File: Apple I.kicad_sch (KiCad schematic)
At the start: 16 parts, among them J4 Processor Bus Connector, SW1 Reset, U1 W65C02SxP, U2 74125, U3 UT62256CPCL, U4 W27C512, U5 SN74HC00N, U6 74154, U7 74HC138, Y1 TXC-7C

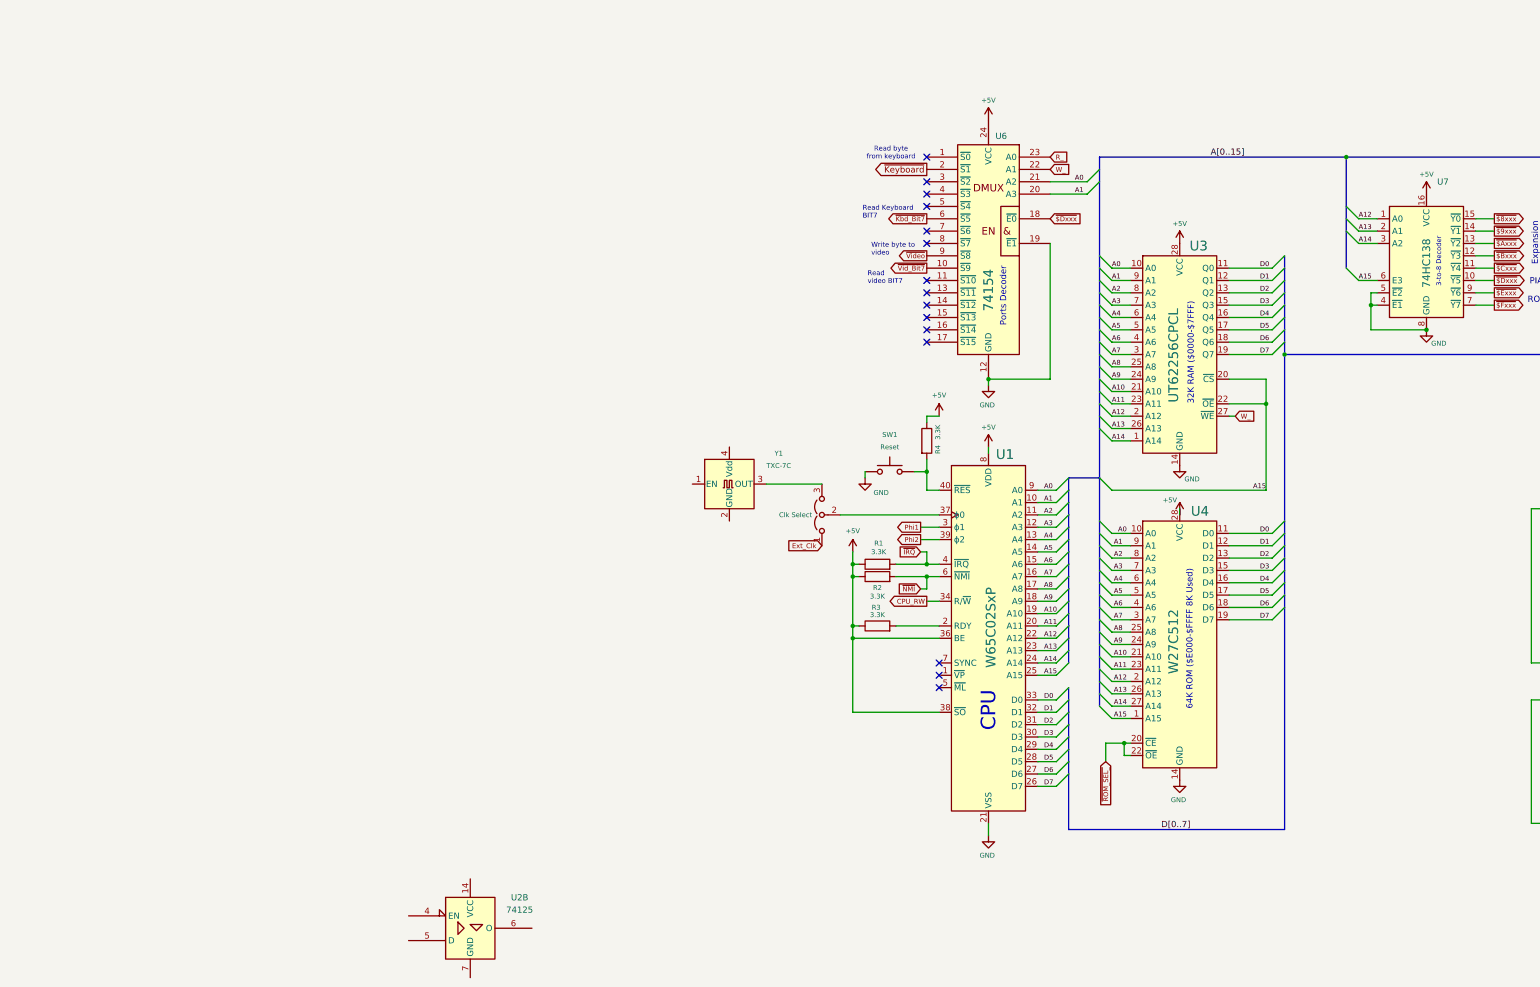
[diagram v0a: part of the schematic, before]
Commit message: Working on Video and Keyboard controllers
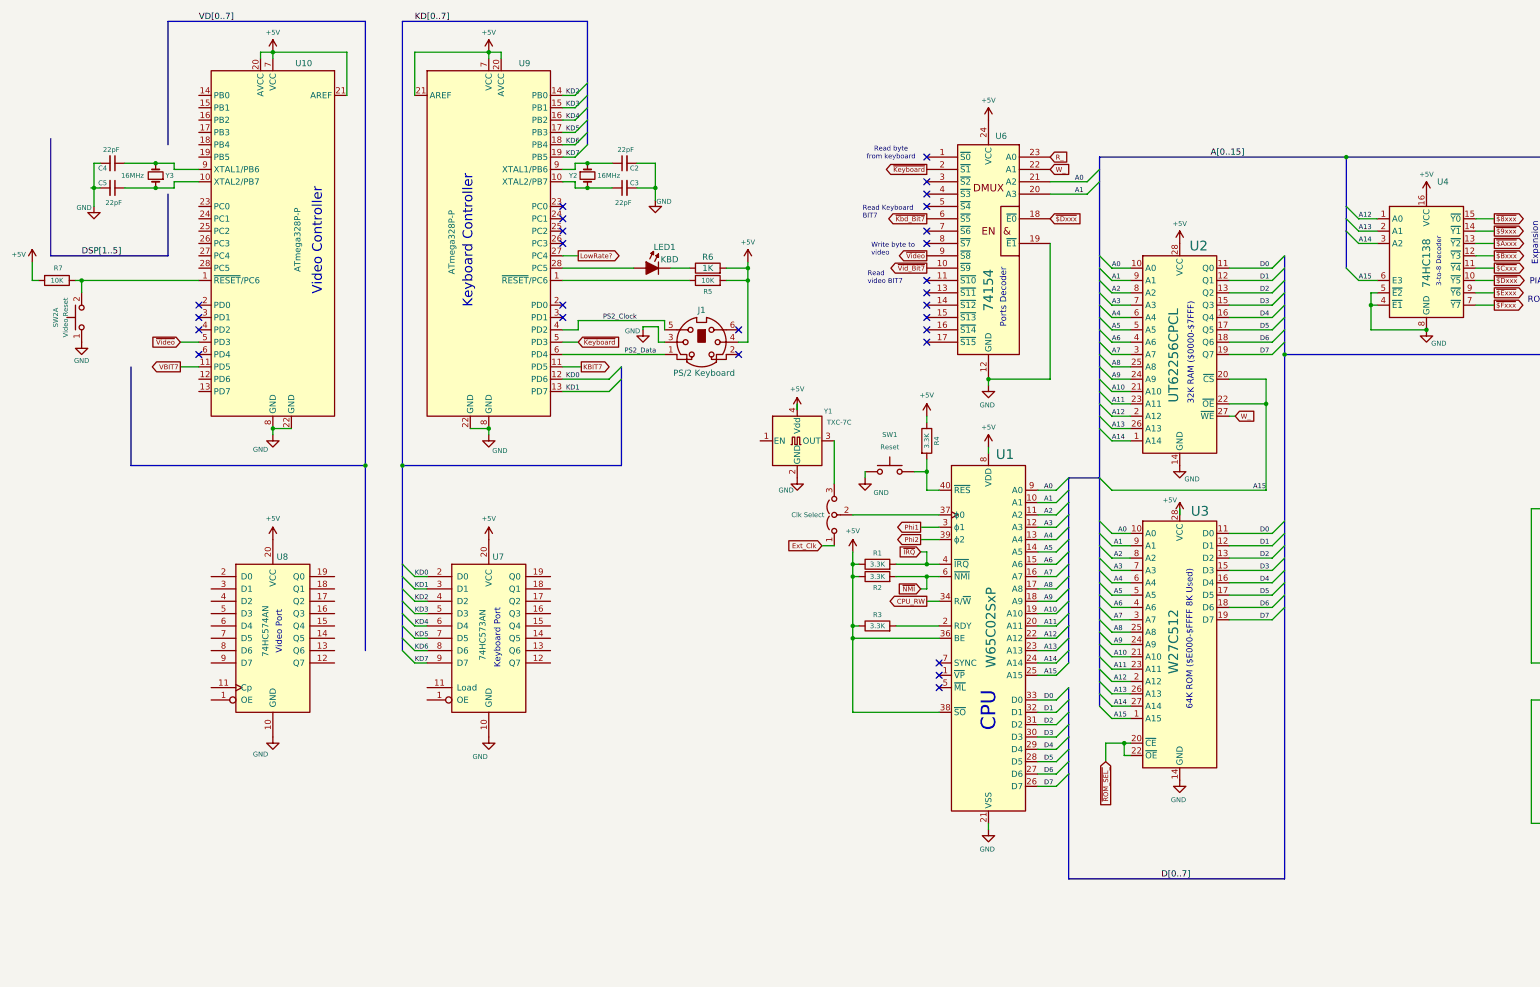
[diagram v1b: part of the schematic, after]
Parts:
- removed U2: 74125, symbol 74xx_IEEE:74125
- added C2, C3, C4, C5: 22pF, symbol Device:C_Small
- added J1: PS/2 Keyboard, symbol Connector:Mini-DIN-6
- added LED1: KBD, PCM_LED_THT_AKL:LED_D2.0mm_W4.8mm_H2.5mm_FlatTop, symbol PCM_LED_AKL:LED_2mm
- added R5, R7: 10K, symbol Device:R
- added R6: 1K, symbol Device:R
- added SW2: Video Reset, symbol Switch:SW_Push_Dual_x2
- added U10, U9: ATmega328P-P, Package_DIP:DIP-28_W7.62mm, symbol MCU_Microchip_ATmega:ATmega328P-P
- added U7: 74HC573AN, symbol 74xx:74LS573
- added U8: 74HC574AN, symbol 74xx:74LS574
- added Y2, Y3: 16MHz, symbol Device:Crystal_Small
- renumbered U3 to U2, U4 to U3, U7 to U4
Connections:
- net +5V: now also Y1.4 (Vdd), J1.4, R5.2, R6.2, R7.2, U10.20 (AVCC), U10.21 (AREF), U10.7 (VCC), U7.20 (VCC), U8.20 (VCC), U9.20 (AVCC), U9.21 (AREF), U9.7 (VCC)
- net GND: now also Y1.2 (GND), C2.2, C3.2, C4.2, C5.2, J1.3, SW2.1 (C), U10.22 (GND), U10.8 (GND), U7.10 (GND), U8.10 (GND), U9.22 (GND), U9.8 (GND)
- net ~{Keyboard}: now also U9.5 (PD3)
- net ~{Video}: now also U10.5 (PD3)
- new net: C3.1, U9.10 (XTAL2/PB7), Y2.2
- new net: R7.1, SW2.2 (D), U10.1 (~{RESET}/PC6)
- new net: C5.1, U10.10 (XTAL2/PB7), Y3.1
- new net: C4.1, U10.9 (XTAL1/PB6), Y3.2
- new net: C2.1, U9.9 (XTAL1/PB6), Y2.1
- new net: R5.1, U9.1 (~{RESET}/PC6)
- new net: LED1.1 (K), R6.1
- new net: LED1.2 (A), U9.28 (PC5)
- new net KBIT7: U9.11 (PD5)
- new net KD0: U7.2 (D0), U9.12 (PD6)
- new net KD1: U7.3 (D1), U9.13 (PD7)
- new net KD2: U7.4 (D2), U9.14 (PB0)
- new net KD3: U7.5 (D3), U9.15 (PB1)
- new net KD4: U7.6 (D4), U9.16 (PB2)
- new net KD5: U7.7 (D5), U9.17 (PB3)
- new net KD6: U7.8 (D6), U9.18 (PB4)
- new net KD7: U7.9 (D7), U9.19 (PB5)
- new net LowRate?: U9.27 (PC4)
- new net PS2_Clock: J1.5, U9.4 (PD2)
- new net PS2_Data: J1.1, U9.6 (PD4)
- new net VBIT7: U10.11 (PD5)
- no-connect marks 15 -> 27
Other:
- note added: "Keyboard Controller"
- note added: "Keyboard Port"
- note added: "Video Controller"
- note added: "Video Port"
- moved on the sheet: Y1

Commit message: Schematic 1.0 add footprints and pcb
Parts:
- removed Y1: TXC-7C, Oscillator:Oscillator_SMD_TXC_7C-4Pin_5.0x3.2mm, symbol Oscillator:TXC-7C
- added C10, C11, C12, C13, C14, C15, C6, C7, C8, C9: .1uF, Capacitor_THT:C_Disc_D5.0mm_W2.5mm_P5.00mm, symbol Device:C_Small
- added JP2, JP3: AREF, Jumper:SolderJumper-2_P1.3mm_Open_RoundedPad1.0x1.5mm, symbol Jumper:SolderJumper_2_Open
- added R10, R11, R12, R8, R9: 10K, Resistor_THT:R_Axial_DIN0207_L6.3mm_D2.5mm_P10.16mm_Horizontal, symbol Device:R
- added unit 2 of SW2
- added TP1: Beep, TestPoint:TestPoint_THTPad_2.0x2.0mm_Drill1.0mm, symbol Connector:TestPoint
- added TP2: MISO, TestPoint:TestPoint_THTPad_2.0x2.0mm_Drill1.0mm, symbol Connector:TestPoint
- added TP3: TV-SDA, TestPoint:TestPoint_THTPad_2.0x2.0mm_Drill1.0mm, symbol Connector:TestPoint
- added TP4: TV-SCL, TestPoint:TestPoint_THTPad_2.0x2.0mm_Drill1.0mm, symbol Connector:TestPoint
- added TP5: LowRateClk, TestPoint:TestPoint_THTPad_2.0x2.0mm_Drill1.0mm, symbol Connector:TestPoint
- added U11: 2.8 TFT SPI 240x320 V1.2, digikey-footprints:TFT-320x240, symbol Driver_Display:CR2013-MI2120
- added U12: SN74AHC125N, Package_DIP:DIP-14_W7.62mm_Socket, symbol dk_Logic-Buffers-Drivers-Receivers-Transceivers:SN74AHCT125N
- added Y1: 1MHz, Oscillator:Oscillator_DIP-8, symbol Oscillator:CXO_DIP8
- C1: value 0.1uF -> .1uF; footprint (none) -> Capacitor_THT:C_Disc_D5.0mm_W2.5mm_P5.00mm
- C2, C3, C4, C5: footprint (none) -> Capacitor_THT:C_Disc_D5.0mm_W2.5mm_P5.00mm
- J1: footprint (none) -> digikey-footprints:MINI-DIN-6-FULL-SHIELD
- J4: footprint (none) -> Connector_PinHeader_2.54mm:PinHeader_2x24_P2.54mm_Vertical
- JP1: footprint (none) -> Connector_PinHeader_2.54mm:PinHeader_1x03_P2.54mm_Vertical
- R1, R2, R3, R4, R5, R6, R7: footprint (none) -> Resistor_THT:R_Axial_DIN0207_L6.3mm_D2.5mm_P10.16mm_Horizontal
- SW1, SW2: footprint (none) -> digikey-footprints:Terminal_Block_D1.3mm_P5mm
- U1: footprint Package_DIP:DIP-40_W15.24mm -> Package_DIP:DIP-40_W15.24mm_Socket
- U10, U9: footprint Package_DIP:DIP-28_W7.62mm -> Package_DIP:DIP-28_W7.62mm_Socket
- U2, U3: footprint Package_DIP:DIP-28_W15.24mm -> Package_DIP:DIP-28_W15.24mm_Socket
- U4: footprint (none) -> Package_DIP:DIP-16_W7.62mm_Socket
- U5: footprint digikey-footprints:DIP-14_W3mm -> Package_DIP:DIP-14_W7.62mm_Socket
- U6: footprint (none) -> Package_DIP:DIP-24_W7.62mm_Socket
- U7, U8: footprint (none) -> Package_DIP:DIP-20_W7.62mm_Socket
- Y2, Y3: footprint (none) -> Crystal:Crystal_HC49-4H_Vertical
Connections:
- net +5V: now also U7.11 (Load), C10.2, C11.2, C12.2, C13.2, C14.2, C15.1, C6.2, C7.2, C8.2, C9.2, JP2.2 (B), JP3.2 (B), U11.1 (VCC), U11.8 (LED), U12.14 (VCC), Y1.8 (Vcc); no longer U10.21 (AREF), U9.21 (AREF)
- net D0: now also U7.19 (Q0), U8.2 (D0)
- net D1: now also U7.18 (Q1), U8.3 (D1)
- net D2: now also U7.17 (Q2), U8.4 (D2)
- net D3: now also U7.16 (Q3), U8.5 (D3)
- net D4: now also U7.15 (Q4), U8.6 (D4)
- net D5: now also U7.14 (Q5), U8.7 (D5)
- net D6: now also U7.13 (Q6), U8.8 (D6)
- net D7: now also U7.12 (Q7), U8.9 (D7), U12.3 (1Y), U12.6 (2Y)
- net GND: now also U8.1 (OE), C10.1, C11.1, C12.1, C13.1, C14.1, C15.2, C6.1, C7.1, C8.1, C9.1, R11.2, U11.2 (GND), U12.7 (GND), Y1.4 (GND)
- net KBIT7: now also U12.5 (2A)
- net VBIT7: now also U12.2 (1A)
- net ~{Kbd_Bit7}: now also U12.4 (2~{OE})
- net ~{Keyboard}: now also U7.1 (OE)
- net ~{Vid_Bit7}: now also U12.1 (1~{OE})
- net ~{Video}: now also U8.11 (Cp)
- net at JP1.3 (B): now also Y1.1 (EN)
- net VD7: now reaches U8.12 (Q7)
- net VD7: now also U10.19 (PB5)
- net VD6: now reaches U8.13 (Q6)
- net VD6: now also U10.18 (PB4)
- net VD5: now reaches U8.14 (Q5)
- net VD5: now also U10.17 (PB3)
- net VD4: now reaches U8.15 (Q4)
- net VD4: now also U10.16 (PB2)
- net VD3: now reaches U8.16 (Q3)
- net VD3: now also U10.15 (PB1)
- net VD2: now reaches U8.17 (Q2)
- net VD2: now also U10.14 (PB0)
- net VD1: now reaches U8.18 (Q1)
- net VD1: now also U10.13 (PD7)
- net VD0: now reaches U8.19 (Q0)
- net VD0: now also U10.12 (PD6)
- net SPI.RST: now reaches U10.23 (PC0)
- net SPI.RST: now also R8.2
- net SPI.DC: now reaches U10.24 (PC1)
- net SPI.DC: now also R12.2
- net SPI.MOSI: now reaches U10.25 (PC2)
- net SPI.MOSI: now also R10.2
- net SPI.SCK: now reaches U10.26 (PC3)
- net SPI.SCK: now also R9.2
- net I2C.SDA: now reaches U10.27 (PC4)
- net I2C.SDA: now also TP3.1
- net I2C.SCL: now reaches U10.28 (PC5)
- net I2C.SCL: now also TP4.1
- net at U10.4 (PD2): now also TP1.1
- net LowRate?: no longer names the net of U9.27 (PC4)
- net LowRate?: now also TP5.1
- new net: R11.1, U11.3 (~{CS})
- new net: TP2.1, U11.9 (MISO)
- new net: JP2.1 (A), U9.21 (AREF)
- new net: R12.1, U11.5 (D/~{C})
- new net: R8.1, U11.4 (RESET)
- new net: JP3.1 (A), U10.21 (AREF)
- new net: R10.1, U11.6 (MOSI)
- new net: R9.1, U11.7 (SCK)
- no-connect marks 27 -> 50
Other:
- moved on the sheet: C1, C2, C3, C4, C5, J1, J4, LED1, R1, R2, R3, R4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

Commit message: Additional pcb layout
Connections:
- net GND: now also J1.7 (Case)
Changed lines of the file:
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@@
 		)
 		(property "Value" "PS/2 Keyboard"
-			(at 176.403 156.21 0)
+			(at 184.658 156.21 0)
 			(effects
 				(font
@@
 		(pin "5"
 		)
+		(pin "7"
+		)
 		(instances
 			(project ""
@@
 					(unit 1)
 				)
+			)
+		)
+	)
+	(symbol
+		(lib_id "power:GND")
+		(at 175.895 157.48 0)
+		(unit 1)
+		(exclude_from_sim no)
+		(in_bom yes)
+		(on_board yes)
+		(dnp no)
+		(property "Reference" "#PWR054"
+			(at 175.895 163.83 0)
+			(effects
+				(font
+					(size 1.27 1.27)
+				)
+				(hide yes)
+			)
+		)
+		(property "Value" "GND"
+			(at 173.736 157.734 0)
+			(effects
+				(font
+					(size 1 1)
+				)
+			)
+		)
+		(property "Footprint" ""
+			(at 175.895 157.48 0)
+			(effects
+				(font
+					(size 1.27 1.27)
+				)
+				(hide yes)
+			)
+		)
+		(property "Datasheet" ""
+			(at 175.895 157.48 0)
+			(effects
+				(font
+					(size 1.27 1.27)
+				)
+				(hide yes)
+			)
+		)
+		(property "Description" "Power symbol creates a global label with name \"GND\" , ground"
+			(at 175.895 157.48 0)
+			(effects
+				(font
+					(size 1.27 1.27)
+				)
+				(hide yes)
+			)
+		)
+		(pin "1"
+		)
+		(instances
+			(project "Apple I"
+				(path "/091ce770-e129-4419-8fb8-0b99f410dc89"
+					(reference "#PWR054")
+					(unit 1)
+				)

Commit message: More work on PCB Placement and routing
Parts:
- added D1, D2: LTA-1000G, digikey-footprints:LED_Bar_Graph_LTA-1000, symbol dk_LEDs-Circuit-Board-Indicators-Arrays-Light-Bars-Bar-Graphs:LTA-1000G
- added H1, H2, H3, H4: Corner, MountingHole:MountingHole_3.2mm_M3, symbol PCM_SL_Mechanical:MountingHole_M3
- added H5, H6, H7, H8: Display, MountingHole:MountingHole_3.2mm_M3, symbol PCM_SL_Mechanical:MountingHole_M3
- added J2: Power Terminal, TerminalBlock_Phoenix:TerminalBlock_Phoenix_PT-1,5-2-5.0-H_1x02_P5.00mm_Horizontal, symbol PCM_SL_Screw_Terminal:Screw_Terminal_2_P5.00mm
- added JP4, JP6: ~{LED En}, Jumper:SolderJumper-2_P1.3mm_Open_RoundedPad1.0x1.5mm, symbol Jumper:SolderJumper_2_Open
- added JP5: LED En, Jumper:SolderJumper-2_P1.3mm_Open_RoundedPad1.0x1.5mm, symbol Jumper:SolderJumper_2_Open
- added RN1, RN3: 1K, Resistor_THT:R_Array_SIP9, symbol Device:R_Network08
- added RN2: 2K, Resistor_THT:R_Array_SIP5, symbol Device:R_Network04
- added TP6, TP7: LED, TestPoint:TestPoint_THTPad_2.0x2.0mm_Drill1.0mm, symbol Connector:TestPoint
- added TP8: ~{LED}, TestPoint:TestPoint_THTPad_2.0x2.0mm_Drill1.0mm, symbol Connector:TestPoint
- J4: footprint Connector_PinHeader_2.54mm:PinHeader_2x24_P2.54mm_Vertical -> Connector_PinHeader_2.54mm:PinHeader_2x24_P2.54mm_Vertical_Counter_Clockwise
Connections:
- net +5V: now also J2.1, JP4.2 (B), JP6.2 (B); no longer J1.4, R5.2, R6.2
- net GND: now also R6.2, J2.2, JP5.1 (A)
- net Phi1: now also D2.10
- net Phi2: now also D2.9
- net R_: now also D2.13
- net W_: now also D2.14
- net ~{$8xxx}: now also D1.11
- net ~{$9xxx}: now also D1.12
- net ~{$Axxx}: now also D1.13
- net ~{$Bxxx}: now also D1.14
- net ~{$Cxxx}: now also D1.15
- net ~{$Dxxx}: now also D1.16
- net ~{$Exxx}: now also D1.17
- net ~{$Fxxx}: now also D1.18
- net ~{Kbd_Bit7}: now also D2.18
- net ~{Keyboard}: now also D2.17
- net ~{ROM_SEL_}: now also D2.15
- net ~{Vid_Bit7}: now also D2.20
- net ~{Video}: now also D2.19
- new net: JP5.2 (B), RN2.1 (common)
- new net: D2.1, RN3.2 (R1)
- new net: D2.11, RN2.4 (R3)
- new net: D2.12, RN2.5 (R4)
- new net: D2.16, TP8.1
- new net: D2.2, RN3.3 (R2)
- new net: D2.3, RN3.4 (R3)
- new net: D2.4, RN3.5 (R4)
- new net: D2.5, RN3.6 (R5)
- new net: D2.6, RN3.7 (R6)
- new net: D2.7, RN3.8 (R7)
- new net: D2.8, RN3.9 (R8)
- new net: JP6.1 (A), RN3.1 (common)
- new net: D1.1, TP7.1
- new net: JP4.1 (A), RN1.1 (common)
- new net: D1.3, RN1.2 (R1)
- new net: D1.4, RN1.3 (R2)
- new net: D1.5, RN1.4 (R3)
- new net: D1.6, RN1.5 (R4)
- new net: D1.7, RN1.6 (R5)
- new net: D1.8, RN1.7 (R6)
- new net: D1.9, RN1.8 (R7)
- new net: D1.10, RN1.9 (R8)
- new net: D1.2, TP6.1
- new net: J1.4, R5.2
- new net: D1.19, RN2.2 (R1)
- new net: D1.20, RN2.3 (R2)
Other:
- moved on the sheet: LED1, R6, TP5

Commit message: First pass routing finished
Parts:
- removed unit 2 of SW2
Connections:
- no-connect marks 50 -> 48
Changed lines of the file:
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@@
 	)
 	(no_connect
-		(at 22.225 252.73)
-	)
-	(no_connect
 		(at 44.45 43.18)
 	)
@@
 	)
 	(no_connect
-		(at 22.225 262.89)
-	)
-	(no_connect
 		(at 224.79 116.205)
 	)
@@
 				)
 			)
-		)
-	)
-	(symbol
-		(lib_id "Switch:SW_Push_Dual_x2")
-		(at 22.225 257.81 90)
-		(unit 2)
-		(exclude_from_sim no)
-		(in_bom yes)
-		(on_board yes)
-		(dnp no)
-		(property "Reference" "SW2"
-			(at 16.891 257.81 0)
-			(effects
-				(font
-					(size 1 1)
-				)
-			)
-		)
-		(property "Value" "Video Reset"
-			(at 18.923 257.81 0)
-			(effects
-				(font
-					(size 1 1)
-				)
-			)
-		)
-		(property "Footprint" "digikey-footprints:Terminal_Block_D1.3mm_P5mm"
-			(at 17.145 257.81 0)
-			(effects
-				(font
-					(size 1.27 1.27)
-				)
-				(hide yes)
-			)
-		)
-		(property "Datasheet" "~"
-			(at 17.145 257.81 0)
-			(effects
-				(font
-					(size 1.27 1.27)
-				)
-				(hide yes)
-			)
-		)
-		(property "Description" "Push button switch, generic, separate symbols, four pins"
-			(at 22.225 257.81 0)
-			(effects
-				(font
-					(size 1.27 1.27)
-				)
-				(hide yes)
-			)
-		)
-		(pin "1"
-		)
-		(pin "3"
-		)
-		(pin "4"
-		)
-		(pin "2"
-		)
-		(instances
-			(project "Apple I"
-				(path "/091ce770-e129-4419-8fb8-0b99f410dc89"
-					(reference "SW2")
-					(unit 2)
-				)
-			)
